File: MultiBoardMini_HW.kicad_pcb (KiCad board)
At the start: 2 copper layers, 63 x 63 mm, 56 parts, among them J1 PB0, J2 PA10, J3 Conn_01x02_Male, J6 Conn_01x04, SW1 PF1, SW2 RESET, SW4 PF1, T1 PTS_1.5_2, T2 PTS_1.5_2, T3 PTS_1.5_2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

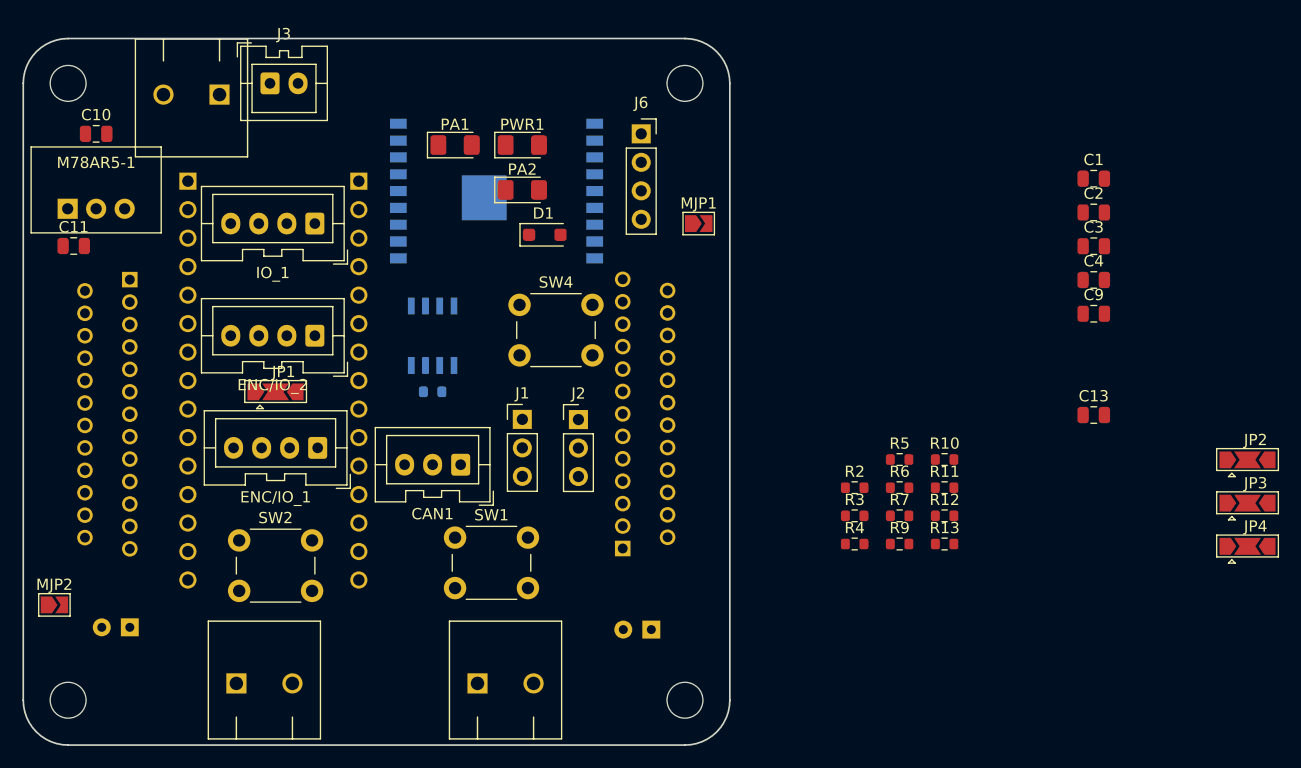
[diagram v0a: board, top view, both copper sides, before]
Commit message: add slide switch footprints
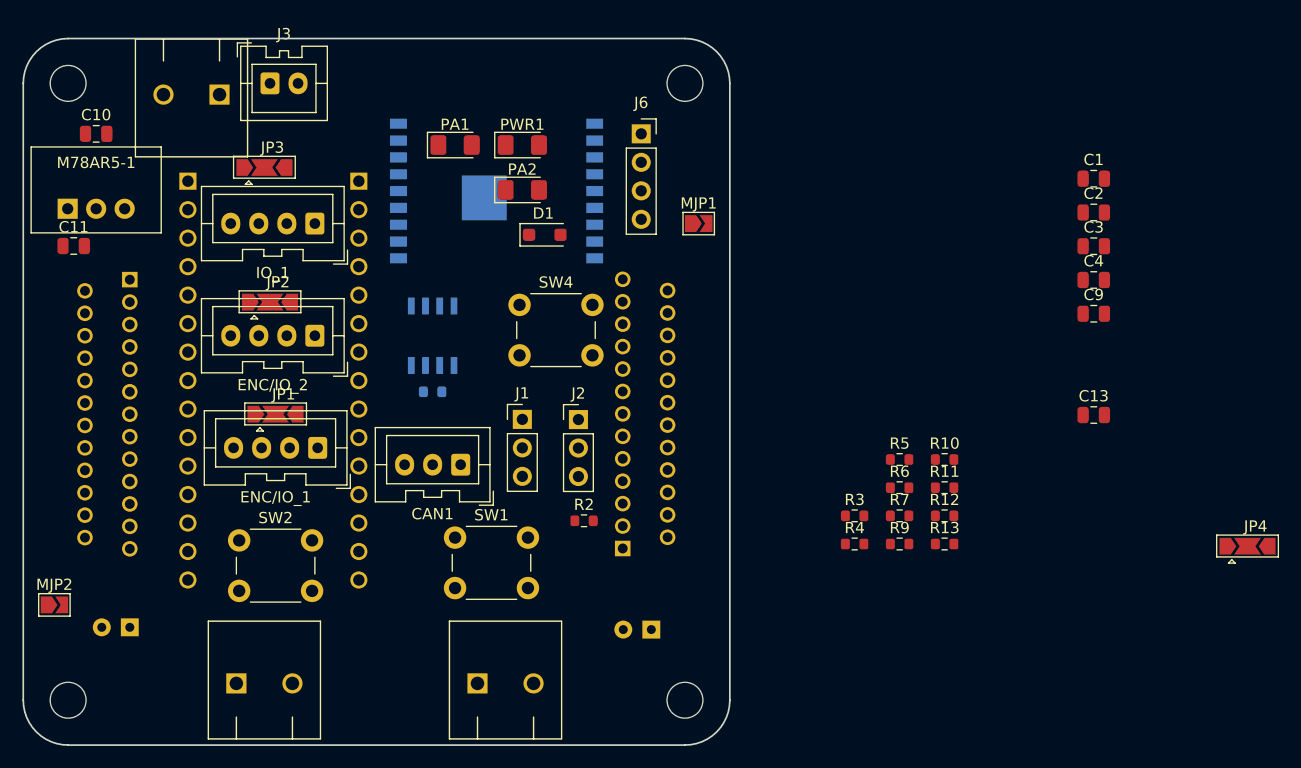
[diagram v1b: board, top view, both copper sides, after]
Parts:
- SW4: value PF1 -> ~
- moved JP3 92.6 mm to (-10.0, -20.0)
- moved JP2 88.3 mm to (-9.50, -8.00)
- moved R2 24.3 mm to (18.5, 11.5)
- moved JP1 2.00 mm to (-9.00, 2.00)
- renumbered T1 to MOTOR1, T2 to MOTOR2
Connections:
- IO_1 pad 4: Net-(ENC/IO_2-Pin_3) -> Net-(IO_1-Pin_4)
- U2 pad 3_1: Net-(U2A-PA9) -> Net-(J6-Pin_2)
- U2 pad 3_10: Net-(SW3-B) -> unconnected-(U2A-PF0-Pad3_10)
- U2 pad 3_14: unconnected-(U2A-PB5-Pad3_14) -> Net-(U2A-PB5)
- U2 pad 3_15: unconnected-(U2A-PB4-Pad3_15) -> Net-(U2A-PB4)
- U2 pad 3_2: Net-(J2-Pin_3) -> Net-(J6-Pin_1)
- U2 pad 3_6: Net-(J1-Pin_3) -> Net-(U2A-PB0)
- U2 pad 3_7: Net-(U2A-PB7) -> Net-(IO_1-Pin_4)
- U2 pad 3_8: Net-(U2A-PB6) -> Net-(IO_1-Pin_3)
- U2 pad 4_10: Net-(J6-Pin_1) -> Net-(J2-Pin_3)
- U2 pad 4_15: unconnected-(U2B-PB3-Pad4_15) -> Net-(SW3-B)
- U2 pad 4_5: Net-(J6-Pin_2) -> unconnected-(U2B-PA2-Pad4_5)
- U2 pad 4_8: Net-(IO_1-Pin_3) -> Net-(U2B-PA5)
- U2 pad 4_9: unconnected-(U2B-PA4-Pad4_9) -> Net-(J1-Pin_3)
- U4 pad 22: Net-(U2A-PA8) -> Net-(U2A-PB1)
- U4 pad 8: Net-(J1-Pin_3) -> Net-(U2A-PB4)
- U4 pad 9: Net-(U2A-PB1) -> Net-(U2B-PA5)
- U5 pad 22: Net-(U2A-PA9) -> Net-(U2A-PB0)
- U5 pad 8: Net-(U2A-PB6) -> Net-(U2A-PA8)
- U5 pad 9: Net-(U2A-PB7) -> Net-(U2A-PB5)

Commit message: Update iroiro
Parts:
- removed JP4: Boot Option, Jumper:SolderJumper-3_P2.0mm_Open_TrianglePad1.0x1.5mm
- removed R10, R11: 10k, Resistor_SMD:R_0603_1608Metric
- added J4: PA10, Connector_PinHeader_2.54mm:PinHeader_1x03_P2.54mm_Vertical, F.Cu at (-19.5, -29.0)
- added SW3: SW_Push_DPDT, MultiBoardMini_Libraries:SSSS213202, F.Cu at (16.0, -1.30)
- added SW5: SW_Push_DPDT, MultiBoardMini_Libraries:SSSS213202, F.Cu at (16.0, 7.20)
- C1, C2, C9, R12, R9: moved to B.Cu
- SW4: footprint Button_Switch_THT:SW_PUSH_6mm_H4.3mm -> Button_Switch_SMD:SW_Push_1P1T_NO_Vertical_Wuerth_434133025816
- moved C3 96.3 mm to (-28.9, 12.5)
- moved C4 93.7 mm to (-29.0, 2.00)
- moved R7 74.8 mm to (-28.0, 15.5)
- moved R3 69.6 mm to (-22.7, -13.0)
- moved C1 62.8 mm to (2.00, -8.55), turned to -90 degrees
- moved R9 59.5 mm to (-1.00, -22.0), turned to 180 degrees
- moved C2 52.4 mm to (12.0, -9.00), turned to -90 degrees
- moved C13 47.2 mm to (18.0, 13.0)
- moved R5 46.7 mm to (6.00, -17.0), turned to 90 degrees
- moved R6 45.0 mm to (9.50, -16.8), turned to 90 degrees
- moved R12 44.3 mm to (22.0, -22.7), turned to -90 degrees
- moved C9 43.7 mm to (22.0, -19.1), turned to -90 degrees
- moved R4 42.0 mm to (14.0, -17.2), turned to 90 degrees
- moved R13 23.1 mm to (28.2, 19.0)
- moved J2 11.9 mm to (8.00, 9.00), turned to -90 degrees
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- renumbered IO_1 to IO_3

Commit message: 部品は一おおむね完了
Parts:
- removed ? (x4): , 
- added REF3: MountingHole_3.2mm_M3, MountingHole:MountingHole_3.2mm_M3, F.Cu at (27.5, -27.5)
- added REF3: MountingHole_3.2mm_M3, MountingHole:MountingHole_3.2mm_M3, F.Cu at (-27.5, -27.5)
- added REF3: MountingHole_3.2mm_M3, MountingHole:MountingHole_3.2mm_M3, F.Cu at (-27.5, 27.5)
- added REF3: MountingHole_3.2mm_M3, MountingHole:MountingHole_3.2mm_M3, F.Cu at (27.5, 27.5)
- C10, C11, C13, C3, C4, JP1, JP2, JP3, MJP1, MJP2, R13, R2, R3, R7, U1: moved to B.Cu
- C9, R12: moved to F.Cu
- SW1, SW2: footprint Button_Switch_THT:SW_PUSH_6mm_H4.3mm -> Button_Switch_SMD:SW_Push_1P1T_NO_6x6mm_H9.5mm
- moved C11 58.4 mm to (19.0, 23.0)
- moved T3 53.3 mm to (0.00, 26.0), turned to 0 degrees
- moved J4 52.0 mm to (2.25, 18.2), turned to -90 degrees
- moved J3 47.9 mm to (1.00, 23.5), turned to 180 degrees
- moved C10 41.9 mm to (4.00, 10.8), turned to -90 degrees
- moved R13 39.3 mm to (23.5, -20.0), turned to 90 degrees
- moved U1 38.9 mm to (1.50, 12.2), turned to 90 degrees
- moved MJP2 36.1 mm to (-26.0, -17.0), turned to 180 degrees
- moved R7 36.1 mm to (-21.5, -20.0), turned to 90 degrees
- moved R2 32.8 mm to (23.5, -16.5), turned to 90 degrees
- moved C4 23.3 mm to (-19.0, 23.0), turned to 180 degrees
- moved R12 18.2 mm to (3.81, -22.8)
- moved C9 18.2 mm to (3.81, -19.1)
- moved C3 12.5 mm to (-18.0, 18.5)
- moved D1 6.16 mm to (3.81, -14.6), turned to 90 degrees
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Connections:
- CAN1 pad 2: unconnected-(CAN1-Pin_2-Pad2) -> Net-(CAN1-Pin_2)
- CAN1 pad 3: unconnected-(CAN1-Pin_3-Pad3) -> Net-(CAN1-Pin_3)
- J1 pad 1: GND -> GNDPWR
- J2 pad 1: GND -> GNDPWR
- R1 pad 1: Net-(U6-CANL) -> Net-(CAN1-Pin_2)
- R1 pad 2: Net-(U6-CANH) -> Net-(CAN1-Pin_3)
- U3 pad 9: (no net) -> GND
- U6 pad 6: Net-(U6-CANL) -> Net-(CAN1-Pin_2)
- U6 pad 7: Net-(U6-CANH) -> Net-(CAN1-Pin_3)
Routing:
- net PWR: track 0.00 -> 142.6 mm
- net Net-(J4-Pin_1): track 0.00 -> 3.81 mm

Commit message: PWR　MOT 配線一旦できた
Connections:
- J1 pad 1: GNDPWR -> GND
- J2 pad 1: GNDPWR -> GND
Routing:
- net GND: track 0.25 -> 202.3 mm, vias 0 -> 1
- net Net-(U5-OUT2A): track 0.00 -> 52.1 mm
- net Net-(U4-OUT1A): track 0.00 -> 51.9 mm
- net Net-(U4-OUT2A): track 0.00 -> 43.1 mm
- net Net-(U5-OUT1A): track 0.00 -> 43.1 mm
- net +5V: track 0.00 -> 2.57 mm

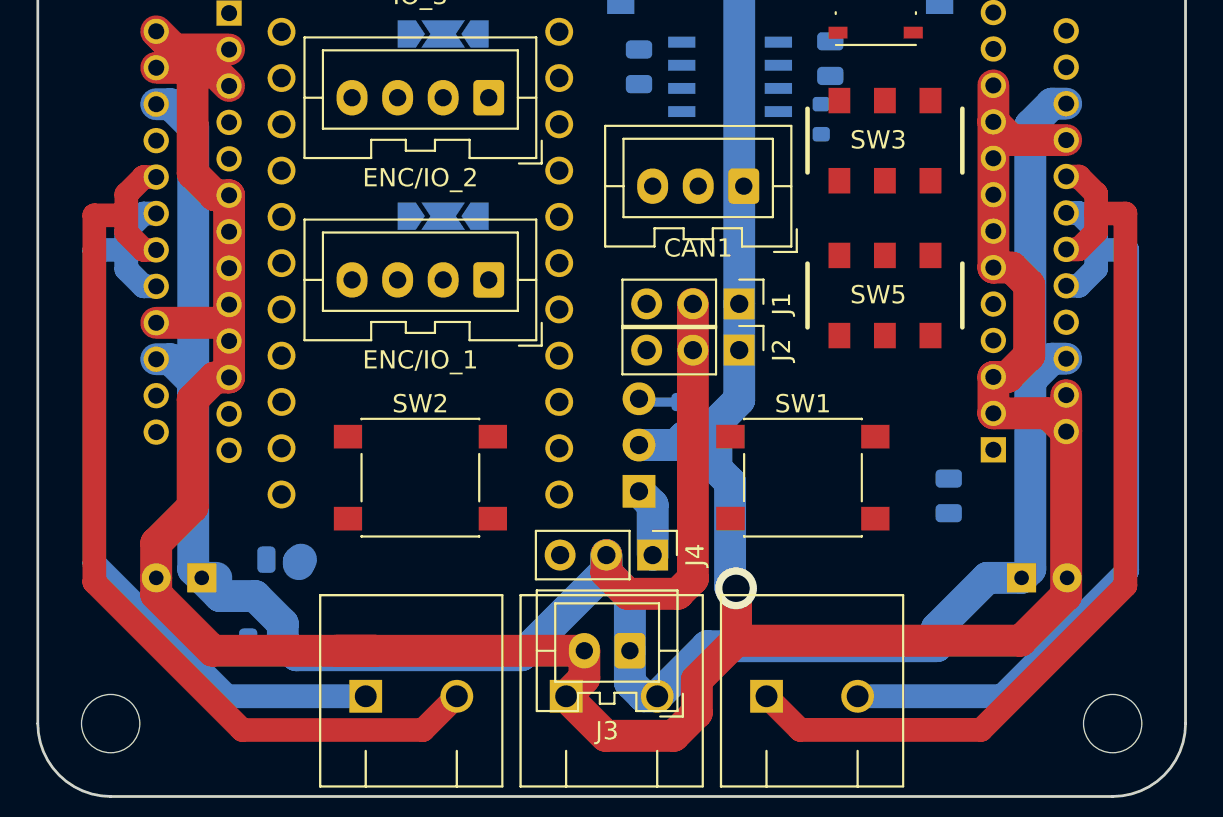
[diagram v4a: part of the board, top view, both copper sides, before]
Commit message: MOT PWR 修正
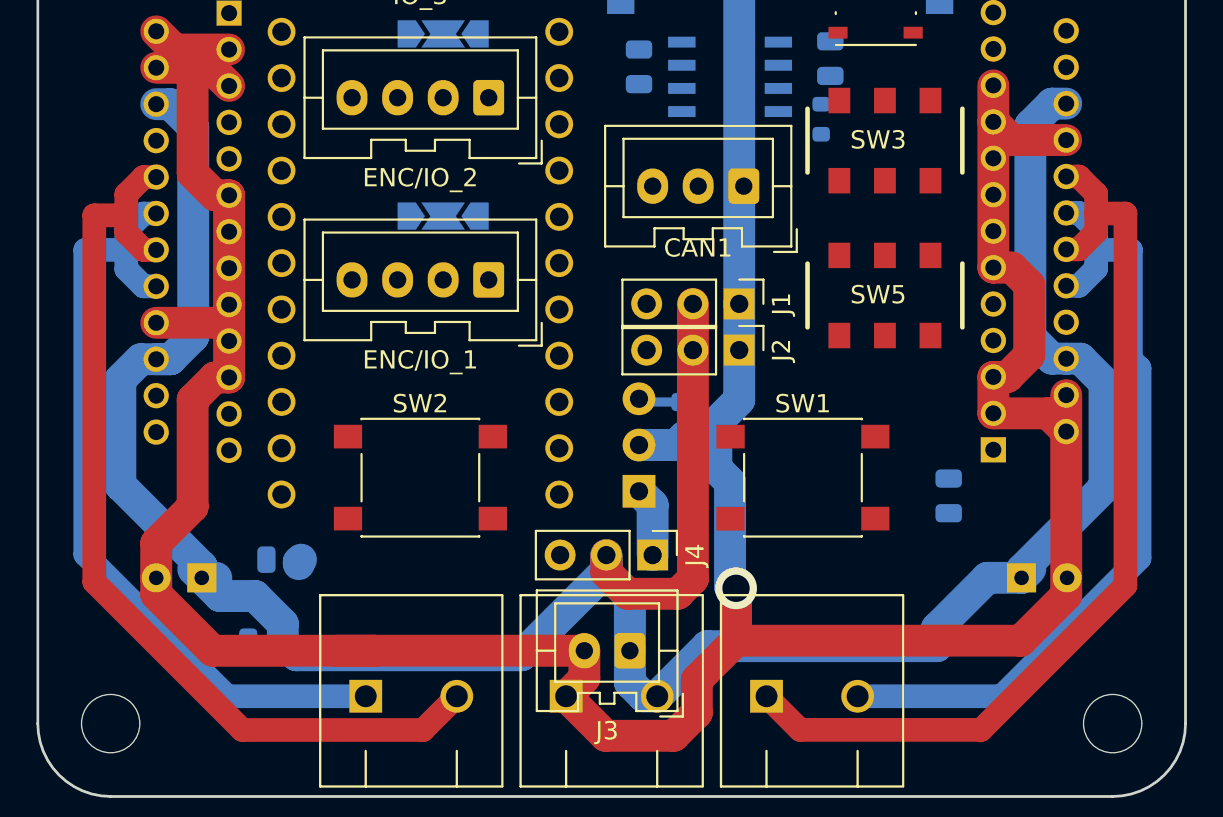
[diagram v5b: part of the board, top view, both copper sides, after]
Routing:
- net PWR: track 143.1 -> 148.0 mm
- net Net-(U5-OUT1A): track 43.1 -> 43.8 mm
- net Net-(U4-OUT2A): track 43.1 -> 43.8 mm
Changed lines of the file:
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@@
   (segment (start 0.871878 20.375) (end 3.628122 20.375) (width 1.75) (layer "F.Cu") (net 4))
   (segment (start -0.29 19.213122) (end 0.871878 20.375) (width 1.75) (layer "F.Cu") (net 4))
-  (segment (start -22.969 9.5) (end -22.969 -5.251796) (width 1.75) (layer "B.Cu") (net 4))
-  (segment (start -22.969 9.5) (end -22.969 8.748204) (width 1.75) (layer "B.Cu") (net 4))
+  (segment (start 22.981 6.283796) (end 22.981 -5.343796) (width 1.75) (layer "B.Cu") (net 4))
   (segment (start -19.568324 20.5) (end -18.05 22.018324) (width 1.75) (layer "B.Cu") (net 4))
+  (segment (start 22.5 19.07262) (end 22.5 19.5) (width 1.75) (layer "B.Cu") (net 4))
   (segment (start 22.5 19.5) (end 22.981 19.019) (width 1.75) (layer "B.Cu") (net 4))
   (segment (start -24.217204 -6.5) (end -25 -6.5) (width 1.75) (layer "B.Cu") (net 4))
   (segment (start -22.5 19.5) (end -22.969 19.031) (width 1.75) (layer "B.Cu") (net 4))
   (segment (start 20.618324 19.5) (end 22.5 19.5) (width 1.75) (layer "B.Cu") (net 4))
+  (segment (start 24.167204 7.47) (end 22.981 6.283796) (width 1.75) (layer "B.Cu") (net 4))
+  (segment (start -26.969 14.406) (end -22.5 18.875) (width 1.75) (layer "B.Cu") (net 4))
   (segment (start 5.25 23.25) (end 17.85 23.25) (width 1.75) (layer "B.Cu") (net 4))
+  (segment (start -25.85 7.5) (end -26.969 8.619) (width 1.75) (layer "B.Cu") (net 4))
   (segment (start 17.85 23.25) (end 17.85 22.268324) (width 1.75) (layer "B.Cu") (net 4))
   (segment (start 1 25.25) (end 1 23.5) (width 1.75) (layer "B.Cu") (net 4))
   (segment (start -22.969 -5.251796) (end -24.217204 -6.5) (width 1.75) (layer "B.Cu") (net 4))
+  (segment (start 24.167204 -6.53) (end 24.95 -6.53) (width 1.75) (layer "B.Cu") (net 4))
   (segment (start 2.5 26) (end 1.75 26) (width 1.75) (layer "B.Cu") (net 4))
-  (segment (start -22.969 19.031) (end -22.969 9.5) (width 1.75) (layer "B.Cu") (net 4))
+  (segment (start 25.732796 7.47) (end 27.05 8.787204) (width 1.75) (layer "B.Cu") (net 4))
   (segment (start 1 23.5) (end 1 20.503122) (width 1.75) (layer "B.Cu") (net 4))
   (segment (start 17.85 22.268324) (end 20.618324 19.5) (width 1.75) (layer "B.Cu") (net 4))
-  (segment (start -22.969 8.748204) (end -24.217204 7.5) (width 1.75) (layer "B.Cu") (net 4))
-  (segment (start 24.167204 7.47) (end 24.95 7.47) (width 1.75) (layer "B.Cu") (net 4))
-  (segment (start 22.981 8.656204) (end 22.981 -5.343796) (width 1.75) (layer "B.Cu") (net 4))
+  (segment (start -22.5 18.875) (end -22.5 19.5) (width 1.75) (layer "B.Cu") (net 4))
+  (segment (start -22.969 -5.251796) (end -22.969 6.251796) (width 1.75) (layer "B.Cu") (net 4))
   (segment (start 2.5 26) (end 5.25 23.25) (width 1.75) (layer "B.Cu") (net 4))
   (segment (start -21.5 20.5) (end -19.568324 20.5) (width 1.75) (layer "B.Cu") (net 4))
   (segment (start -0.29 18.25) (end -0.29 19.095344) (width 1.75) (layer "B.Cu") (net 4))
   (segment (start 1 20.503122) (end -0.29 19.213122) (width 1.75) (layer "B.Cu") (net 4))
-  (segment (start 22.981 -5.343796) (end 24.167204 -6.53) (width 1.75) (layer "B.Cu") (net 4))
   (segment (start -17.3 23.75) (end -18.05 23) (width 1.75) (layer "B.Cu") (net 4))
+  (segment (start -26.969 8.619) (end -26.969 14.406) (width 1.75) (layer "B.Cu") (net 4))
+  (segment (start 24.95 7.47) (end 25.732796 7.47) (width 1.75) (layer "B.Cu") (net 4))
   (segment (start -0.29 19.095344) (end -4.944656 23.75) (width 1.75) (layer "B.Cu") (net 4))
-  (segment (start 22.981 19.019) (end 22.981 8.656204) (width 1.75) (layer "B.Cu") (net 4))
+  (segment (start -24.217204 7.5) (end -25.85 7.5) (width 1.75) (layer "B.Cu") (net 4))
+  (segment (start 27.05 8.787204) (end 27.05 14.52262) (width 1.75) (layer "B.Cu") (net 4))
   (segment (start -21.7 19.5) (end -22.5 19.5) (width 1.75) (layer "B.Cu") (net 4))
   (segment (start -24.217204 7.5) (end -25 7.5) (width 1.75) (layer "B.Cu") (net 4))
   (segment (start 1.75 26) (end 1 25.25) (width 1.75) (layer "B.Cu") (net 4))
-  (segment (start 24.167204 -6.53) (end 24.95 -6.53) (width 1.75) (layer "B.Cu") (net 4))
   (segment (start -0.29 19.213122) (end -0.29 18.25) (width 1.75) (layer "B.Cu") (net 4))
-  (segment (start 22.981 8.656204) (end 24.167204 7.47) (width 1.75) (layer "B.Cu") (net 4))
   (segment (start -4.944656 23.75) (end -17.3 23.75) (width 1.75) (layer "B.Cu") (net 4))
+  (segment (start -22.969 6.251796) (end -24.217204 7.5) (width 1.75) (layer "B.Cu") (net 4))
+  (segment (start 22.981 -5.343796) (end 24.167204 -6.53) (width 1.75) (layer "B.Cu") (net 4))
+  (segment (start 27.05 14.52262) (end 22.5 19.07262) (width 1.75) (layer "B.Cu") (net 4))
   (segment (start -22.5 19.5) (end -21.5 20.5) (width 1.75) (layer "B.Cu") (net 4))
   (segment (start -18.05 22.018324) (end -18.05 23) (width 1.75) (layer "B.Cu") (net 4))
+  (segment (start 24.95 7.47) (end 24.167204 7.47) (width 1.75) (layer "B.Cu") (net 4))
   (segment (start 26.594 -0.5) (end 28.2 -0.5) (width 1.3) (layer "F.Cu") (net 48))
   (segment (start 10.34507 27.84507) (end 8.5 26) (width 1.3) (layer "F.Cu") (net 48))
@@
   (segment (start 28.2 -0.5) (end 28.2 19.925484) (width 1.3) (layer "F.Cu") (net 48))
   (segment (start 26.594 -1.58) (end 26.594 -0.5) (width 1.3) (layer "F.Cu") (net 48))
+  (segment (start 28.5 1.5) (end 28.5 7.514842) (width 1.3) (layer "B.Cu") (net 49))
   (segment (start 25.644 -0.53) (end 24.95 -0.53) (width 1.3) (layer "B.Cu") (net 49))
-  (segment (start 28.3 1.5) (end 28.3 19.1) (width 1.3) (layer "B.Cu") (net 49))
+  (segment (start 28.5 7.514842) (end 28.975 7.989843) (width 1.3) (layer "B.Cu") (net 49))
   (segment (start 21.4 26) (end 13.5 26) (width 1.3) (layer "B.Cu") (net 49))
   (segment (start 26.594 2.52) (end 26.594 1.5) (width 1.3) (layer "B.Cu") (net 49))
   (segment (start 25.644 3.47) (end 26.594 2.52) (width 1.3) (layer "B.Cu") (net 49))
-  (segment (start 26.594 1.5) (end 28.3 1.5) (width 1.3) (layer "B.Cu") (net 49))
   (segment (start 26.594 0.42) (end 25.644 -0.53) (width 1.3) (layer "B.Cu") (net 49))
   (segment (start 24.95 3.47) (end 25.644 3.47) (width 1.3) (layer "B.Cu") (net 49))
   (segment (start 26.594 1.5) (end 26.594 0.42) (width 1.3) (layer "B.Cu") (net 49))
-  (segment (start 28.3 19.1) (end 21.4 26) (width 1.3) (layer "B.Cu") (net 49))
-  (segment (start -28.4 1.5) (end -28.4 18.709182) (width 1.3) (layer "B.Cu") (net 50))
+  (segment (start 26.594 1.5) (end 28.5 1.5) (width 1.3) (layer "B.Cu") (net 49))
+  (segment (start 28.975 7.989843) (end 28.975 18.425) (width 1.3) (layer "B.Cu") (net 49))
+  (segment (start 28.975 18.425) (end 21.4 26) (width 1.3) (layer "B.Cu") (net 49))
+  (segment (start -28.894 1.5) (end -28.894 18.215182) (width 1.3) (layer "B.Cu") (net 50))
   (segment (start -25.694 3.5) (end -26.644 2.55) (width 1.3) (layer "B.Cu") (net 50))
+  (segment (start -28.894 18.215182) (end -21.109182 26) (width 1.3) (layer "B.Cu") (net 50))
   (segment (start -26.644 2.55) (end -26.644 1.5) (width 1.3) (layer "B.Cu") (net 50))
   (segment (start -21.109182 26) (end -13.5 26) (width 1.3) (layer "B.Cu") (net 50))
-  (segment (start -26.644 1.5) (end -28.4 1.5) (width 1.3) (layer "B.Cu") (net 50))
+  (segment (start -26.644 1.5) (end -28.894 1.5) (width 1.3) (layer "B.Cu") (net 50))
   (segment (start -26.644 1.5) (end -26.644 0.45) (width 1.3) (layer "B.Cu") (net 50))
   (segment (start -25.694 -0.5) (end -25 -0.5) (width 1.3) (layer "B.Cu") (net 50))
   (segment (start -26.644 0.45) (end -25.694 -0.5) (width 1.3) (layer "B.Cu") (net 50))
   (segment (start -25 3.5) (end -25.694 3.5) (width 1.3) (layer "B.Cu") (net 50))
-  (segment (start -28.4 18.709182) (end -21.109182 26) (width 1.3) (layer "B.Cu") (net 50))
   (segment (start -26.644 0.55) (end -25.694 1.5) (width 1.3) (layer "F.Cu") (net 51))
   (segment (start -26.644 -0.4) (end -26.644 0.55) (width 1.3) (layer "F.Cu") (net 51))

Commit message: 自動配線前のいろいろごにょごにょしたやつ
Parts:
- C1, C2, U6: moved to F.Cu
- moved D1 8.08 mm to (5.50, -22.5)
- moved R1 7.93 mm to (4.00, -8.25), turned to 180 degrees
- moved C10 6.30 mm to (6.45, 5.00), turned to 180 degrees
- moved U6 6.25 mm to (4.75, -14.0), turned to -90 degrees
- moved C1 5.34 mm to (0.50, -13.8)
- moved U1 5.23 mm to (5.00, 8.32), turned to 0 degrees
- moved C2 5.20 mm to (9.00, -13.2)
- moved J1 4.96 mm to (7.00, -0.50)
- moved J2 4.96 mm to (7.00, 2.04)
- moved CAN1 4.25 mm to (7.25, -6.25)
- moved C9 3.98 mm to (3.00, -23.0)
- moved R12 3.37 mm to (3.00, -19.5)
- moved SW3 2.26 mm to (14.8, -6.75)
- moved SW4 1.60 mm to (13.5, -12.8)
- moved R9 1.19 mm to (-2.00, -23.2)
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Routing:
- net +3V3: track 0.00 -> 64.5 mm
- net GND: track 202.3 -> 154.5 mm, vias 1 -> 0
- net Net-(CAN1-Pin_2): track 0.00 -> 8.73 mm, vias 0 -> 1
- net Net-(CAN1-Pin_3): track 0.00 -> 6.40 mm, vias 0 -> 1
- net Net-(J4-Pin_1): track 3.81 -> 0.00 mm
- net Net-(IO_3-Pin_2): track 0.00 -> 3.50 mm
- net Net-(ENC/IO_2-Pin_2): track 0.00 -> 3.50 mm
- net Net-(ENC/IO_1-Pin_2): track 0.00 -> 3.50 mm
- net +5V: track 2.57 -> 3.38 mm
